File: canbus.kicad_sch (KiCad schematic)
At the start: 10 parts, among them U1 MCP2518FD, U2 MCP2562FD, Y1 40 MHz

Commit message: updates to BOM and fixes for ERC
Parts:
- C4, C5: MPN CL21C100CBANNNC -> GMC31X5R476M25NT
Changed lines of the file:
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@@
 			)
 		)
-		(property "MPN" "CL21C100CBANNNC"
+		(property "MPN" "GMC31X5R476M25NT"
 			(at 106.68 74.93 0)
 			(hide yes)
@@
 			)
 		)
-		(property "MPN" "CL21C100CBANNNC"
+		(property "MPN" "GMC31X5R476M25NT"
 			(at 106.68 80.01 0)
 			(hide yes)

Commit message: updates to BOM
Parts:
- C4, C5: MPN GMC31X5R476M25NT -> CL21C100CBANNNC
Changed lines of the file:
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@@
 			)
 		)
-		(property "MPN" "GMC31X5R476M25NT"
+		(property "MPN" "CL21C100CBANNNC"
 			(at 106.68 74.93 0)
 			(hide yes)
@@
 			)
 		)
-		(property "MPN" "GMC31X5R476M25NT"
+		(property "MPN" "CL21C100CBANNNC"
 			(at 106.68 80.01 0)
 			(hide yes)

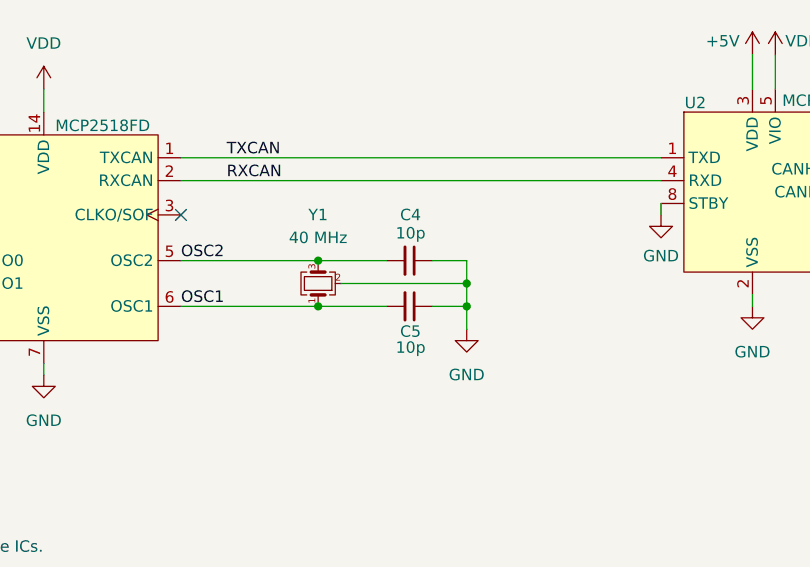
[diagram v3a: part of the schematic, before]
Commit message: Rename references, update symbols and schematic layout
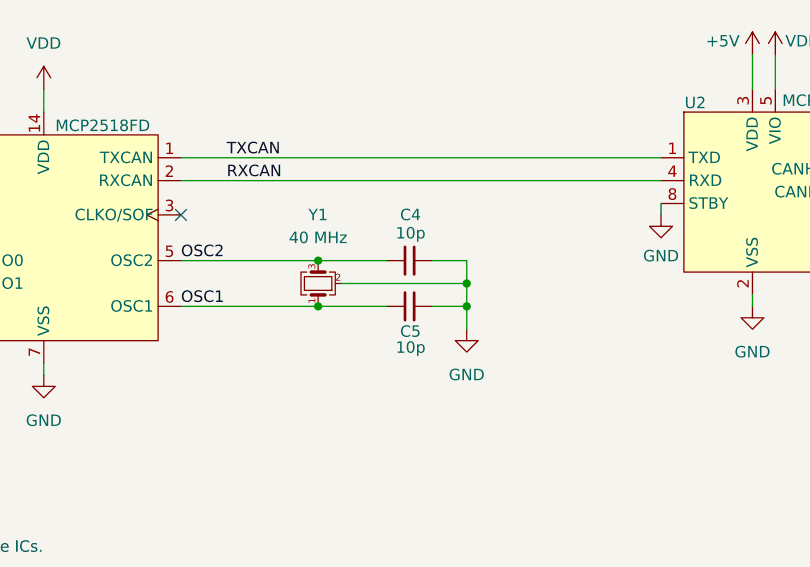
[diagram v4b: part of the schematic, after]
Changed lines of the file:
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@@
 	)
 	(symbol
+		(lib_name "C_Small_1")
 		(lib_id "Device:C_Small")
 		(at 106.68 74.93 270)
@@
 			)
 		)
-		(property "Description" "10pF 50V C0G/NP0 0805"
+		(property "Description" "Unpolarized capacitor, small symbol"
 			(at 106.68 74.93 0)
 			(hide yes)
@@
 			)
 		)
-		(property "Description" "10pF 50V C0G/NP0 0805"
+		(property "Description" "Unpolarized capacitor, small symbol"
 			(at 106.68 80.01 0)
 			(hide yes)
